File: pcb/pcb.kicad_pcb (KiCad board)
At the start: 2 copper layers, 51 parts, among them J1 USB_C_Receptacle_USB2.0, J2 Conn_01x05, SW1 SW_Push, SW2 SW_Push, U1 XC6206P332MR, U2 SRV05-4, U3 DRV5056A3xDBZxQ1, U4 DRV5056A3xDBZxQ1, U5 DRV5056A3xDBZxQ1, U6 RP2040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

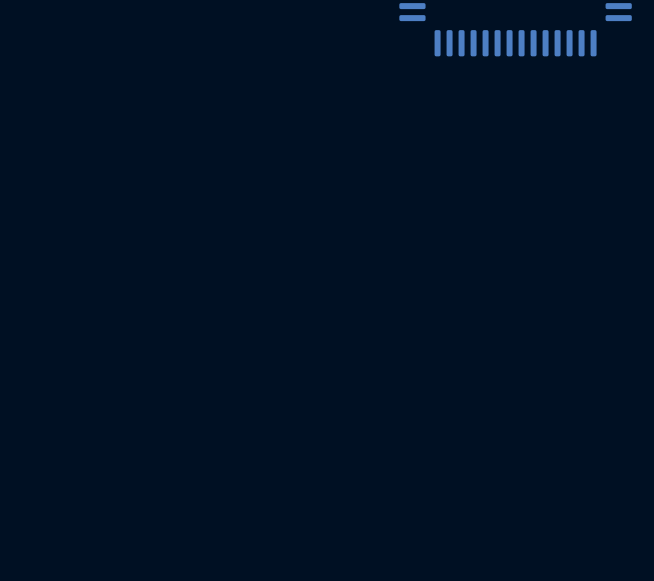
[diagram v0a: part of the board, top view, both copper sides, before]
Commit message: feat: add rgb underglow
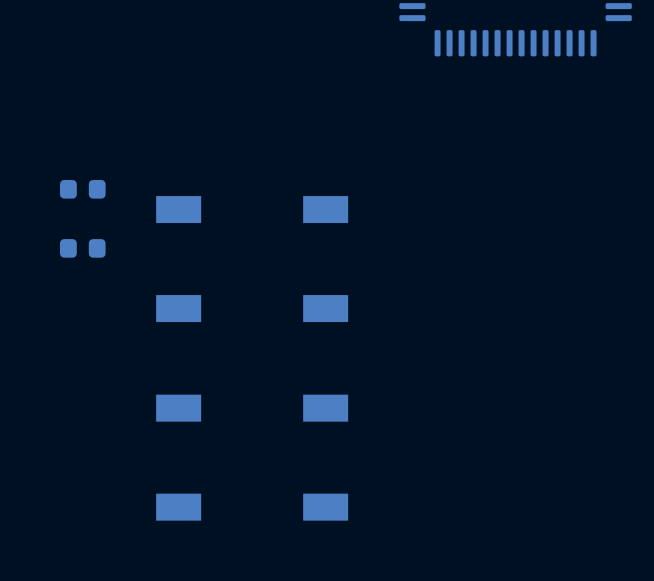
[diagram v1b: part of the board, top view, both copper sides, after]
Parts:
- added C24: 100nF, Capacitor_SMD:C_0402_1005Metric, B.Cu at (17.5, 79.1)
- added C25: 100nF, Capacitor_SMD:C_0402_1005Metric, B.Cu at (17.5, 81.1)
- added D1: WS2812B, LED_SMD:LED_WS2812B_PLCC4_5.0x5.0mm_P3.2mm, B.Cu at (23.1, 81.4)
- added D2: WS2812B, LED_SMD:LED_WS2812B_PLCC4_5.0x5.0mm_P3.2mm, B.Cu at (23.1, 88.0)

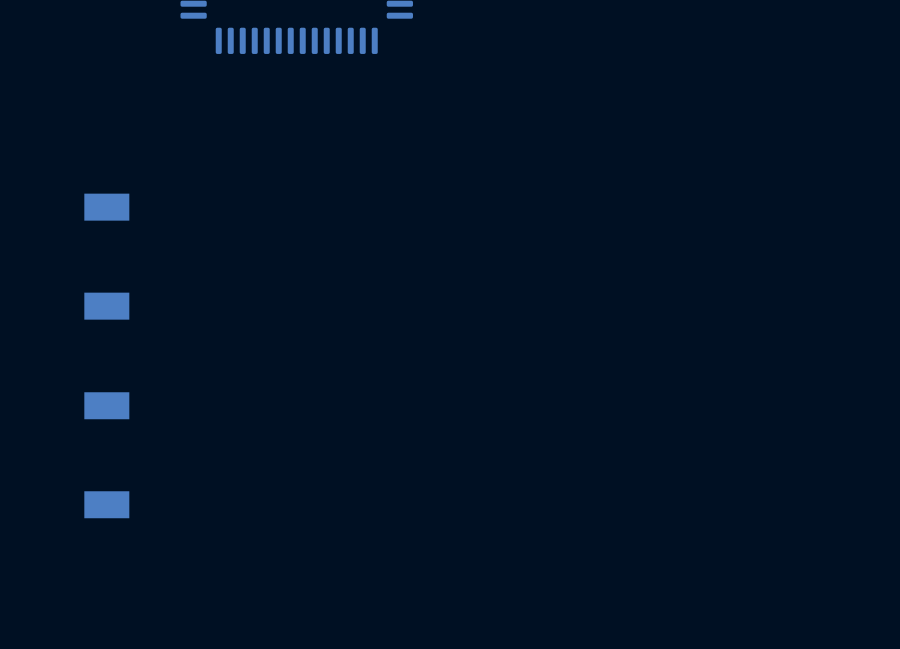
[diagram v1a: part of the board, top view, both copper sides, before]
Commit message: feat: add in-switch leds
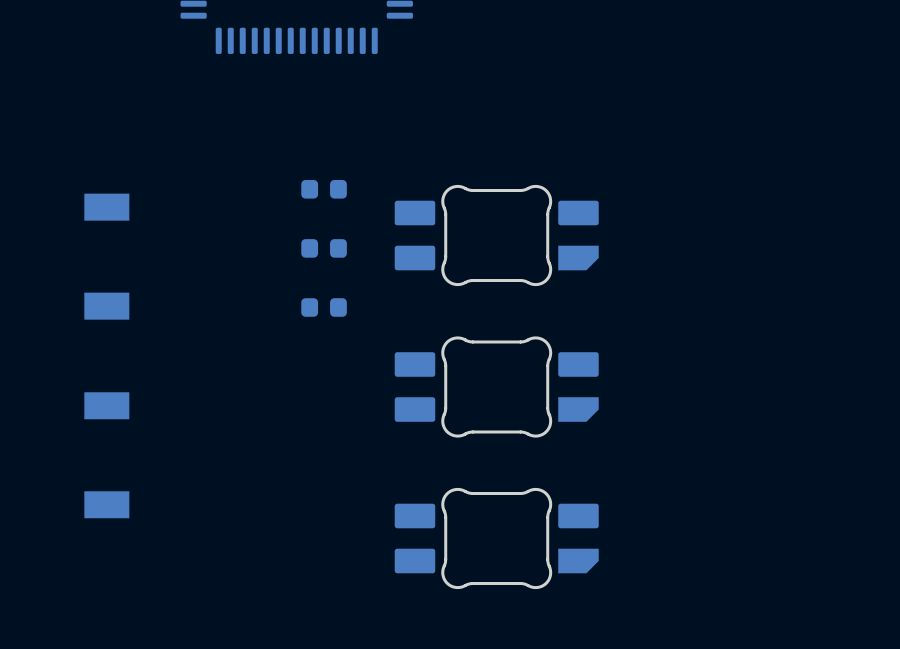
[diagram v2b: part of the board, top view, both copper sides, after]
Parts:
- added C26: 100nF, Capacitor_SMD:C_0402_1005Metric, B.Cu at (32.8, 79.2)
- added C27: 100nF, Capacitor_SMD:C_0402_1005Metric, B.Cu at (32.8, 81.1)
- added C28: 100nF, Capacitor_SMD:C_0402_1005Metric, B.Cu at (32.8, 83.1)
- added LED1: SK6812MINI-E, PCM_marbastlib-various:LED_6028R, B.Cu at (38.5, 80.7)
- added LED2: SK6812MINI-E, PCM_marbastlib-various:LED_6028R, B.Cu at (38.5, 85.8)
- added LED3: SK6812MINI-E, PCM_marbastlib-various:LED_6028R, B.Cu at (38.5, 90.8)
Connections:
- U6 pad 2: unconnected-(U6-GPIO0-Pad2) -> RGB_GLOW
- U6 pad 3: unconnected-(U6-GPIO1-Pad3) -> RGB_HS0
- U6 pad 4: unconnected-(U6-GPIO2-Pad4) -> RGB_HS1
- U6 pad 5: unconnected-(U6-GPIO3-Pad5) -> RGB_HS2
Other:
- board outline added: 3.6 x 3.3 mm

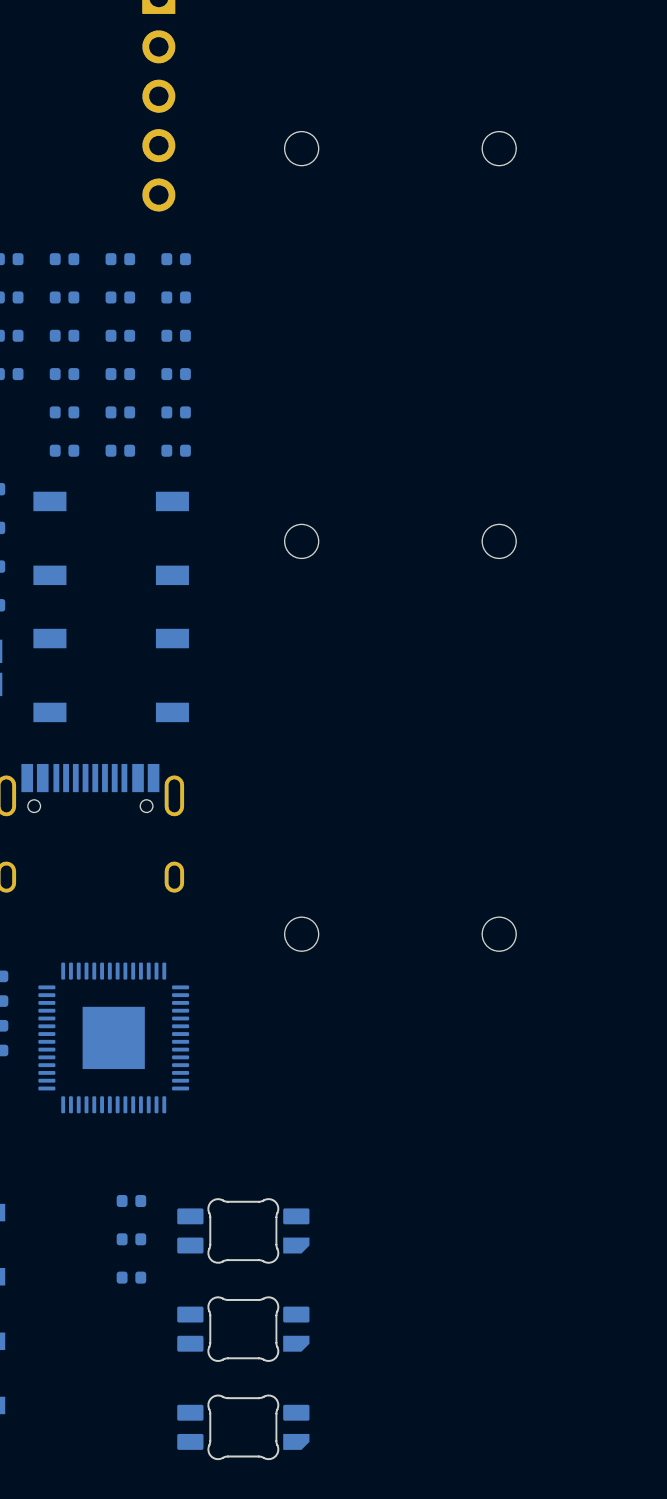
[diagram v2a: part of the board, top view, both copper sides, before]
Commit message: refactor: use marbastlib footprint for in-switch LED
to make it easier to align.
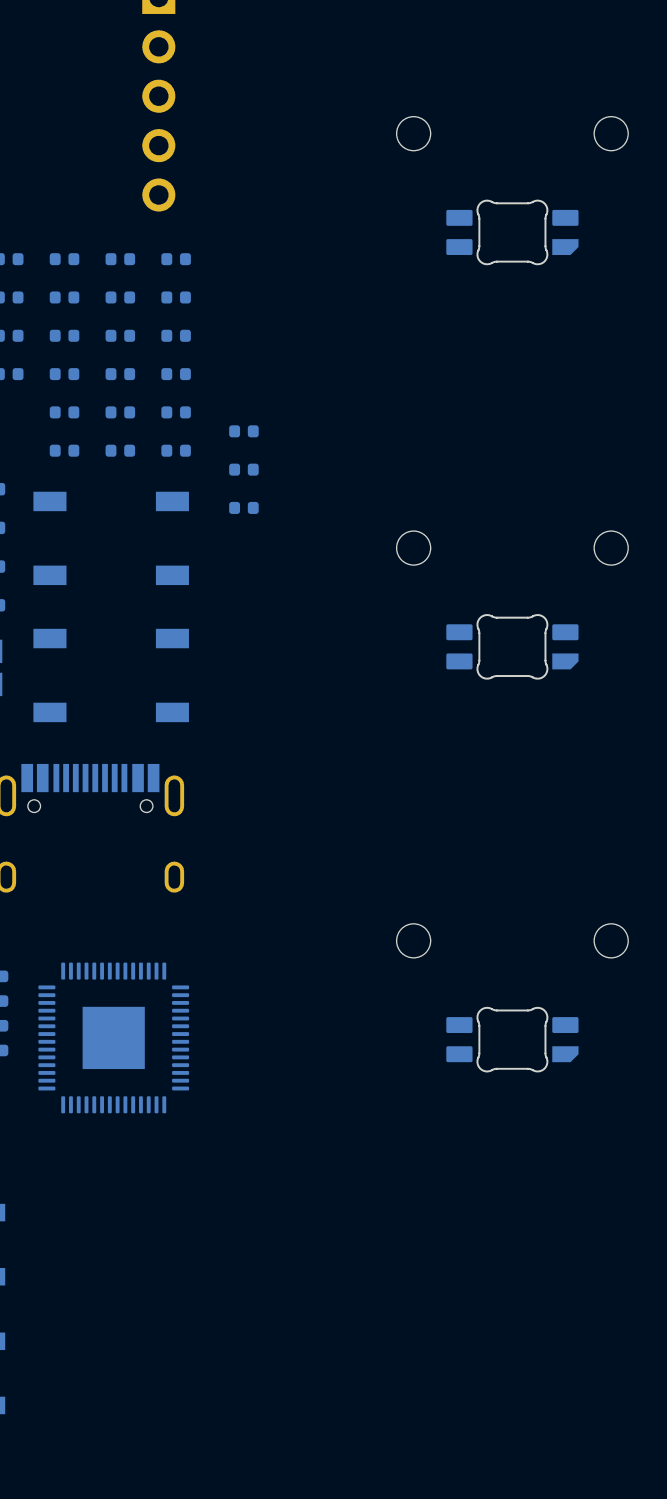
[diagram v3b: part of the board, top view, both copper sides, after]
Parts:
- LED1, LED2, LED3: footprint PCM_marbastlib-various:LED_6028R -> PCM_marbastlib-mx:LED_MX_6028R
- moved LED1 53.2 mm to (52.4, 29.4)
- moved C26 40.0 mm to (38.6, 39.6)
- moved C27 40.0 mm to (38.6, 41.6)
- moved C28 40.0 mm to (38.6, 43.5)
- moved LED2 37.7 mm to (52.4, 50.7)
- moved LED3 24.3 mm to (52.4, 70.9)
- moved H1 5.81 mm to (52.4, 24.3)
- moved H2 5.77 mm to (52.4, 45.6)
- moved H3 5.77 mm to (52.4, 65.8)

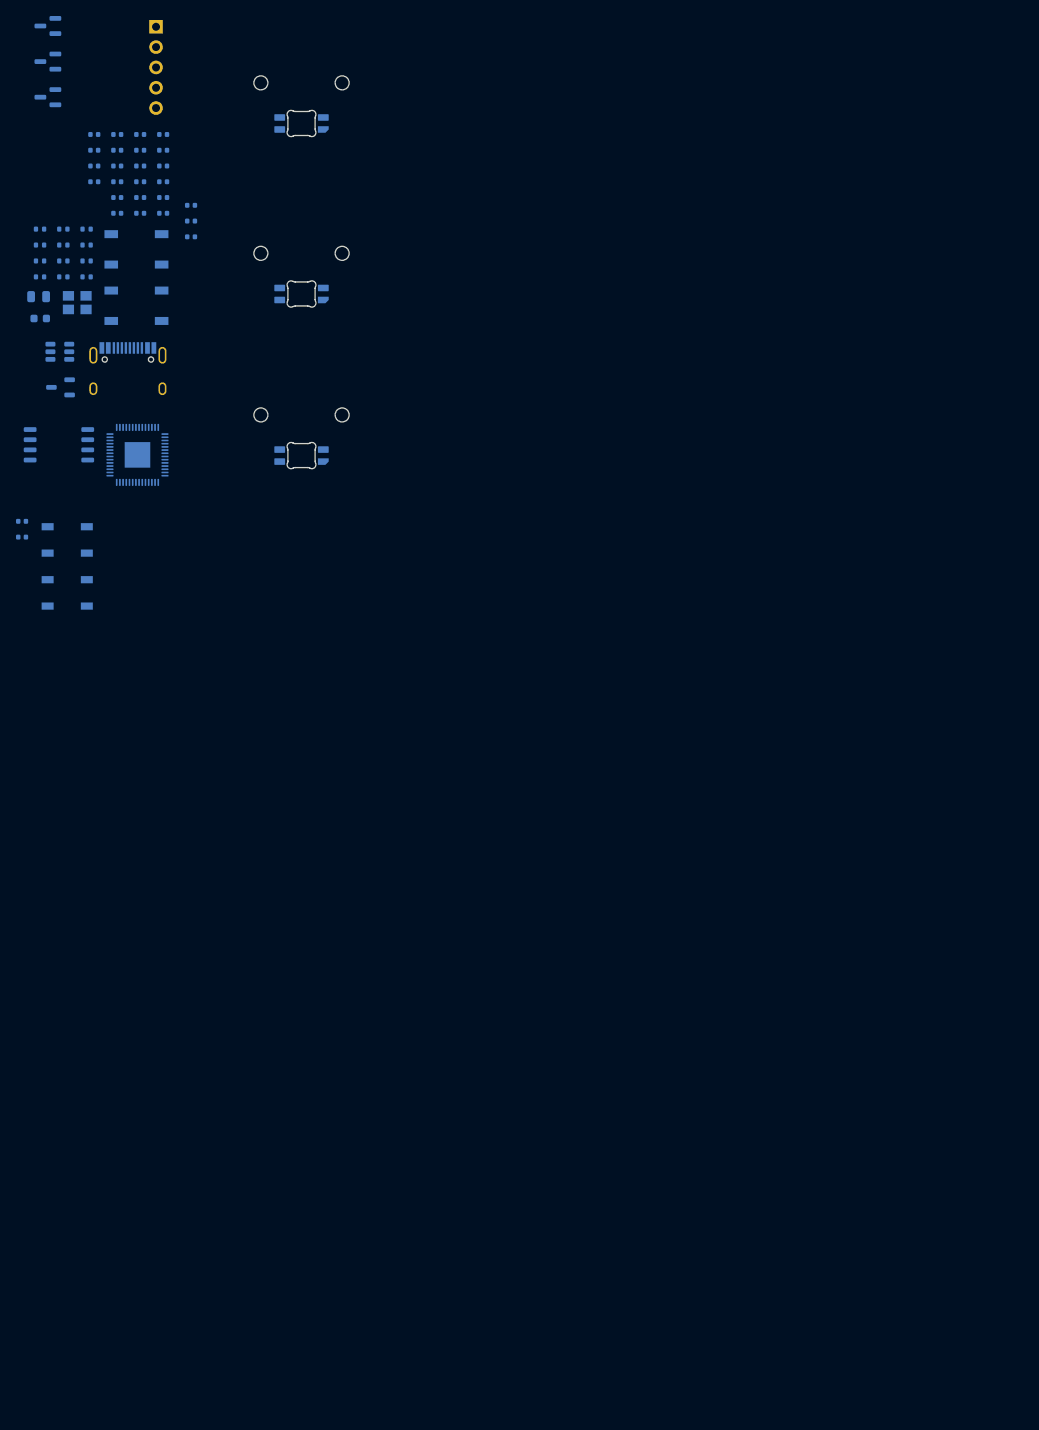
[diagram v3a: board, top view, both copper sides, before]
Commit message: feat: initial attempt at laying out pcb
routing will be tricky - might need a 4 layer pcb due to the mixed voltages...

probably better to remove the in-switch LEDs for the time being...
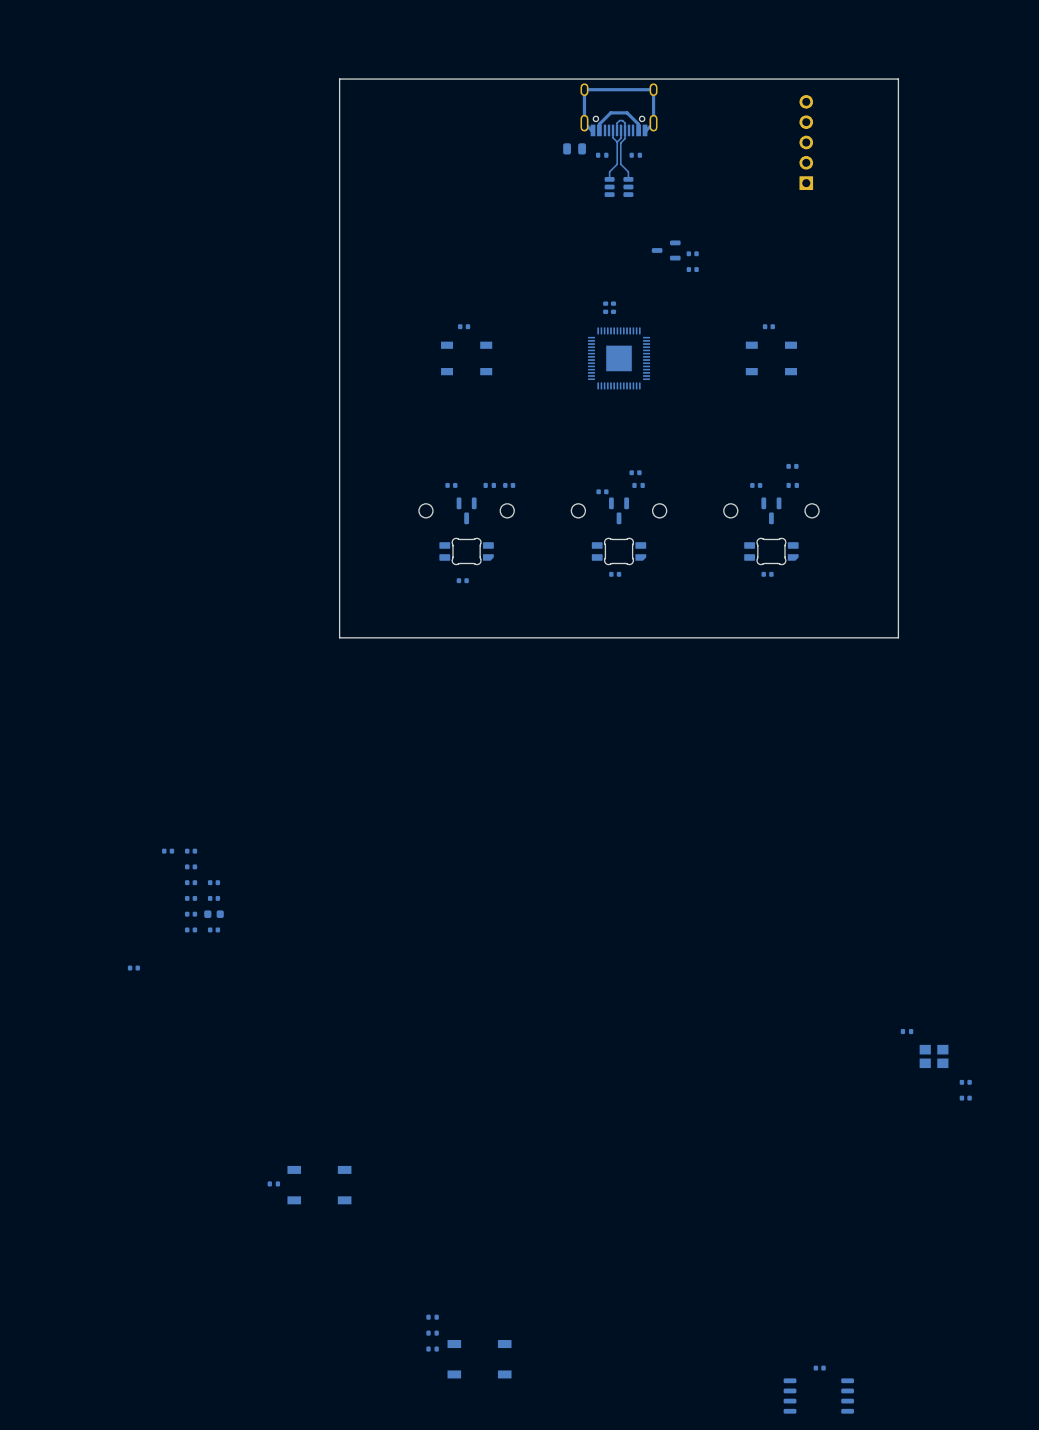
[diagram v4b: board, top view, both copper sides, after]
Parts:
- C10, C18, C2, C20, C22, C3: value 1uF -> 100nF
- C12: value 100nF -> 10uF; footprint Capacitor_SMD:C_0402_1005Metric -> Capacitor_SMD:C_0603_1608Metric
- C13, C26, C28, C8: value 100nF -> 1uF
- C19: value 22pF -> 100nF
- C21: value 22pF -> 1uF
- C24, C25: value 100nF -> 22pF
- C9: value 10uF -> 1uF; footprint Capacitor_SMD:C_0603_1608Metric -> Capacitor_SMD:C_0402_1005Metric
- R5: value 1k -> 27
- R6: value 5k1 -> 27
- R7: value 27 -> 1k
- R8: value 27 -> 100
- R9: value 100 -> 5k1
- moved C28 161.8 mm to (117.2, 184.9)
- moved U7 152.2 mm to (117.0, 188.4)
- moved R7 142.8 mm to (128.1, 142.9)
- moved R10 142.7 mm to (68.8, 178.6)
- moved R12 142.7 mm to (68.8, 182.6)
- moved R11 142.7 mm to (68.8, 180.6)
- moved Y1 142.7 mm to (131.5, 146.0)
- moved SW2 138.5 mm to (74.6, 183.8)
- moved C24 137.2 mm to (135.4, 149.2)
- moved C25 137.2 mm to (135.4, 151.2)
- moved R9 122.9 mm to (48.9, 161.9)
- moved SW1 119.2 mm to (54.6, 162.1)
- moved U5 104.2 mm to (111.1, 77.8), turned to -90 degrees
- moved R8 94.8 mm to (113.8, 74.6)
- moved D2 92.8 mm to (111.1, 58.7)
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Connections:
- C10 pad 1: +3V3 -> +1V1
- C11 pad 1: +3V3 -> +1V1
- C18 pad 1: GND -> +3V3
- C18 pad 2: HS1 -> GND
- C19 pad 1: GND -> +3V3
- C19 pad 2: XIN -> GND
- C2 pad 1: +5V -> GND
- C2 pad 2: GND -> +5V
- C21 pad 2: Net-(C21-Pad2) -> HS1
- C22 pad 2: HS2 -> +5V
- C24 pad 2: +5V -> XIN
- C25 pad 2: +5V -> Net-(C25-Pad2)
- C26 pad 2: +5V -> HS2
- C28 pad 1: GND -> +3V3
- C28 pad 2: +5V -> GND
- C3 pad 1: +3V3 -> GND
- C3 pad 2: GND -> +5V
- C4 pad 1: GND -> +5V
- C4 pad 2: HS0 -> GND
- C6 pad 1: +1V1 -> GND
- C6 pad 2: GND -> HS0
- C7 pad 1: +1V1 -> GND
- C7 pad 2: GND -> +5V
- C8 pad 1: +1V1 -> +3V3
- C9 pad 1: +3V3 -> +1V1
- R5 pad 1: Net-(C21-Pad2) -> D+
- R5 pad 2: XOUT -> Net-(U6-USB_DP)
- R6 pad 1: +3V3 -> D-
- R6 pad 2: RESET -> Net-(U6-USB_DM)
- R7 pad 1: D+ -> Net-(C25-Pad2)
- R7 pad 2: Net-(U6-USB_DP) -> XOUT
- R8 pad 1: D- -> Net-(U5-OUT)
- R8 pad 2: Net-(U6-USB_DM) -> HS2
- R9 pad 1: Net-(U5-OUT) -> +3V3
- R9 pad 2: HS2 -> RESET
- Y1 pad 1: Net-(C21-Pad2) -> Net-(C25-Pad2)
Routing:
- net GND: track 0.00 -> 19.9 mm
- net D+: track 0.00 -> 9.82 mm
- net D-: track 0.00 -> 8.37 mm
- net VBUS: track 0.00 -> 7.62 mm
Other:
- board size 3.6 x 3.3 mm -> 69.8 x 69.8 mm
